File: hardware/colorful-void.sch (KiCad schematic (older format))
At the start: 4 parts, among them J1 Raspberry_Pi_Zero, J2 Barrel_Jack, J3 Conn_01x03, U1 74AHCT125

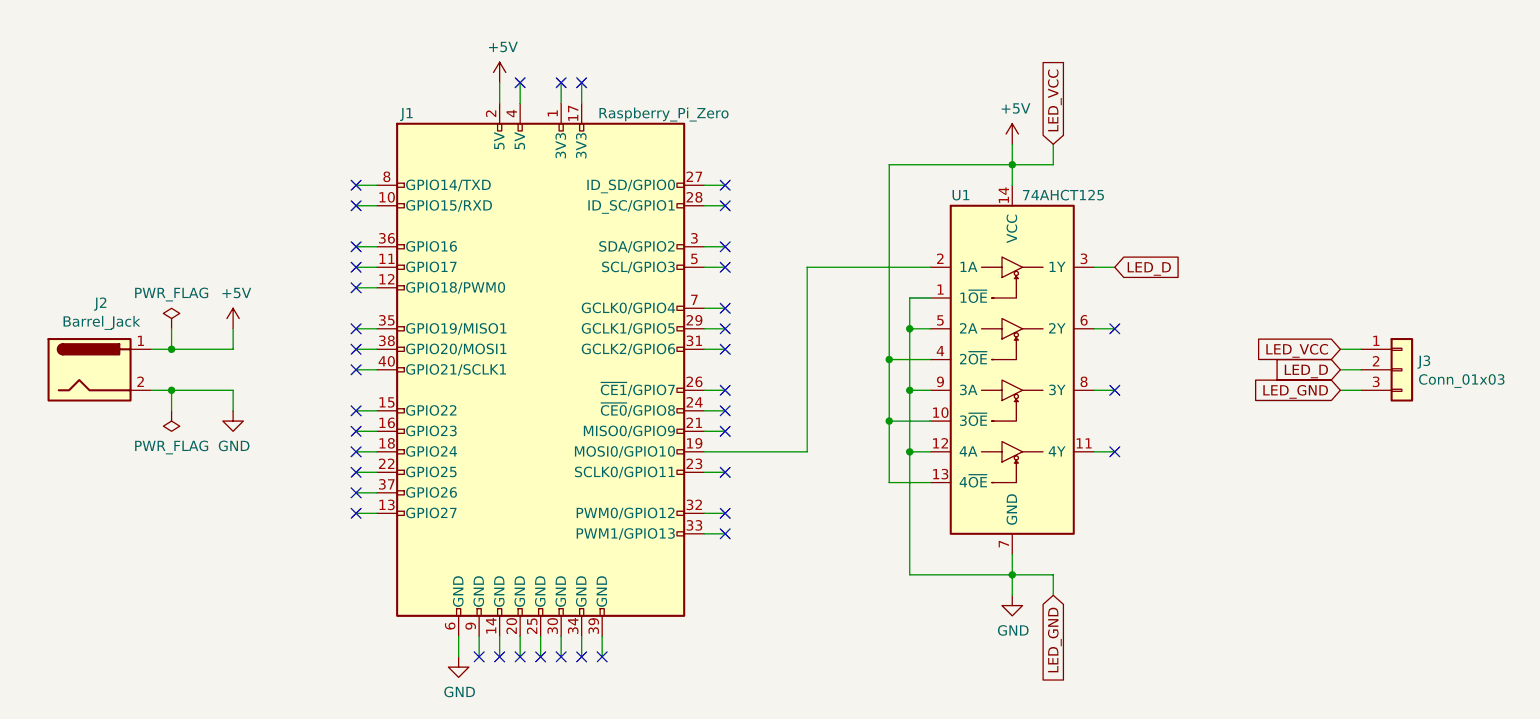
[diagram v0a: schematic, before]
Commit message: Connect client to RGB strip
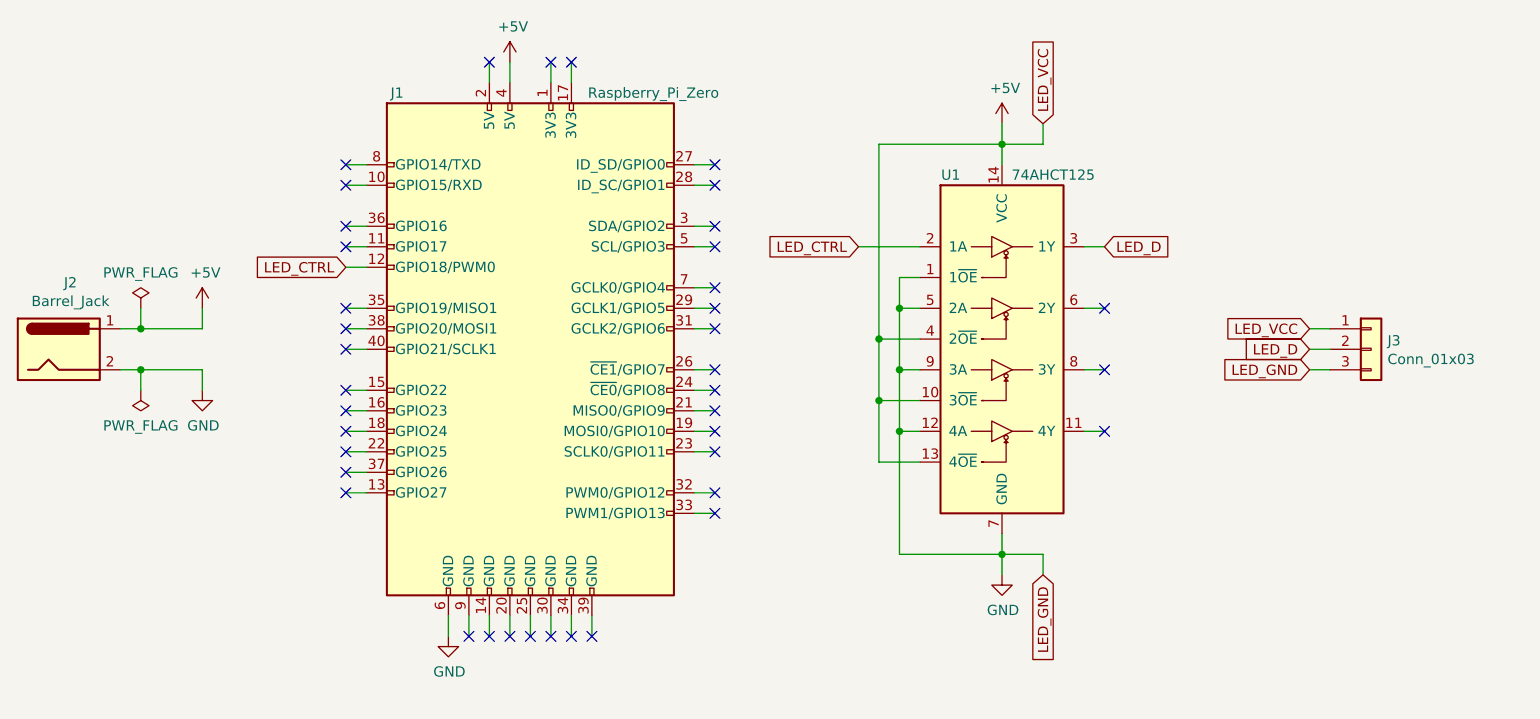
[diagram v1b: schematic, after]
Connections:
- net +5V: now also J1.4 (5V); no longer J1.2 (5V)
- net LED_CTRL: now reaches J1.12 (GPIO18/PWM0)
- net LED_CTRL: now also U1.2 (1A)
- net at J1.19 (MOSI0/GPIO10): no longer U1.2 (1A)
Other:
- moved on the sheet: J1, J2, J3, U1

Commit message: PCB rev. 1
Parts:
- removed J2: Barrel_Jack, symbol Connector:Barrel_Jack
- added H1, H2: MountingHole, misc_hardware:MountingHole_M2.5, symbol Mechanical:MountingHole
- added J2: Conn_01x02, misc_hardware:TerminalBlock_Kaweei_1x02_P2.54mm_Horizontal, symbol Connector_Generic:Conn_01x02
- added NT1: Net-Tie_2, NetTie:NetTie-2_SMD_Pad0.5mm, symbol Device:Net-Tie_2
- J1: footprint (none) -> Connector_PinHeader_2.54mm:PinHeader_2x06_P2.54mm_Vertical
- J3: footprint (none) -> misc_hardware:TerminalBlock_Kaweei_1x03_P2.54mm_Horizontal
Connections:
- net +5V: now also J2.2 (Pin_2), NT1.2; no longer U1.10 (3~OE), U1.13 (4~OE), U1.4 (2~OE)
- net GND: now also J3.2 (Pin_2), J2.1 (Pin_1); no longer J3.3 (Pin_3)
- net LED_D: now also J3.3 (Pin_3); no longer J3.2 (Pin_2)
- new net: NT1.1, U1.10 (3~OE), U1.13 (4~OE), U1.4 (2~OE)
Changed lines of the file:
@@
 F 0 "J1" H 4250 5050 50  0000 C CNN
 F 1 "Raspberry_Pi_Zero" H 5500 5050 50  0000 C CNN
-F 2 "" H 4900 3800 50  0001 C CNN
+F 2 "Connector_PinHeader_2.54mm:PinHeader_2x06_P2.54mm_Vertical" H 4900 3800 50  0001 C CNN
 F 3 "https://www.raspberrypi.org/documentation/hardware/raspberrypi/schematics/rpi_SCH_3bplus_1p0_reduced.pdf" H 4900 3800 50  0001 C CNN
 	1    4900 3800
@@
 	6700 3450 6700 3600
 Wire Wire Line
-	6700 4800 7200 4800
-Wire Wire Line
 	6700 3450 6800 3450
 Connection ~ 6700 3600
@@
 Connection ~ 6600 3750
 Wire Wire Line
-	6600 3750 6600 2800
+	6600 3750 6600 3100
 Connection ~ 6600 4050
 Wire Wire Line
@@
 NoConn ~ 5000 2400
 NoConn ~ 5100 2400
-$Comp
-L Connector:Barrel_Jack J2
-U 1 1 5FDE4F93
-P 2600 3800
-F 0 "J2" H 2657 4125 50  0000 C CNN
-F 1 "Barrel_Jack" H 2657 4034 50  0000 C CNN
-F 2 "" H 2650 3760 50  0001 C CNN
-F 3 "~" H 2650 3760 50  0001 C CNN
-	1    2600 3800
-	1    0    0    -1
-$EndComp
-Wire Wire Line
-	2900 3700 3000 3700
-Wire Wire Line
-	3000 3700 3000 3600
-Wire Wire Line
-	2900 3900 3000 3900
-Wire Wire Line
-	3000 3900 3000 4000
+Wire Wire Line
+	2900 3750 3000 3750
+Wire Wire Line
+	3000 3750 3000 3650
+Wire Wire Line
+	2900 3850 3000 3850
+Wire Wire Line
+	3000 3850 3000 3950
 $Comp
 L power:+5V #PWR03
 U 1 1 5FDEBA13
-P 3300 3600
-F 0 "#PWR03" H 3300 3450 50  0001 C CNN
-F 1 "+5V" H 3315 3773 50  0000 C CNN
-F 2 "" H 3300 3600 50  0001 C CNN
-F 3 "" H 3300 3600 50  0001 C CNN
-	1    3300 3600
+P 3300 3650
+F 0 "#PWR03" H 3300 3500 50  0001 C CNN
+F 1 "+5V" H 3315 3823 50  0000 C CNN
+F 2 "" H 3300 3650 50  0001 C CNN
+F 3 "" H 3300 3650 50  0001 C CNN
+	1    3300 3650
 	1    0    0    -1
 $EndComp
@@
 L power:GND #PWR04
 U 1 1 5FDEC1C7
-P 3300 4000
-F 0 "#PWR04" H 3300 3750 50  0001 C CNN
-F 1 "GND" H 3305 3827 50  0000 C CNN
-F 2 "" H 3300 4000 50  0001 C CNN
-F 3 "" H 3300 4000 50  0001 C CNN
-	1    3300 4000
+P 3300 3950
+F 0 "#PWR04" H 3300 3700 50  0001 C CNN
+F 1 "GND" H 3305 3777 50  0000 C CNN
+F 2 "" H 3300 3950 50  0001 C CNN
+F 3 "" H 3300 3950 50  0001 C CNN
+	1    3300 3950
 	1    0    0    -1
 $EndComp
@@
 L power:PWR_FLAG #FLG01
 U 1 1 5FDF5B6E
-P 3000 3600
-F 0 "#FLG01" H 3000 3675 50  0001 C CNN
-F 1 "PWR_FLAG" H 3000 3773 50  0000 C CNN
-F 2 "" H 3000 3600 50  0001 C CNN
-F 3 "~" H 3000 3600 50  0001 C CNN
-	1    3000 3600
-	1    0    0    -1
-$EndComp
-Wire Wire Line
-	3300 3600 3300 3700
-Wire Wire Line
-	3300 3700 3000 3700
-Connection ~ 3000 3700
-Wire Wire Line
-	3300 4000 3300 3900
-Wire Wire Line
-	3300 3900 3000 3900
-Connection ~ 3000 3900
+P 3000 3650
+F 0 "#FLG01" H 3000 3725 50  0001 C CNN
+F 1 "PWR_FLAG" H 3000 3823 50  0000 C CNN
+F 2 "" H 3000 3650 50  0001 C CNN
+F 3 "~" H 3000 3650 50  0001 C CNN
+	1    3000 3650
+	1    0    0    -1
+$EndComp
+Wire Wire Line
+	3300 3650 3300 3750
+Wire Wire Line
+	3300 3750 3000 3750
+Connection ~ 3000 3750
+Wire Wire Line
+	3300 3950 3300 3850
+Wire Wire Line
+	3300 3850 3000 3850
+Connection ~ 3000 3850
 $Comp
 L power:PWR_FLAG #FLG02
 U 1 1 5FDFB526
-P 3000 4000
-F 0 "#FLG02" H 3000 4075 50  0001 C CNN
-F 1 "PWR_FLAG" H 3000 4173 50  0000 C CNN
-F 2 "" H 3000 4000 50  0001 C CNN
-F 3 "~" H 3000 4000 50  0001 C CNN
-	1    3000 4000
+P 3000 3950
+F 0 "#FLG02" H 3000 4025 50  0001 C CNN
+F 1 "PWR_FLAG" H 3000 4123 50  0000 C CNN
+F 2 "" H 3000 3950 50  0001 C CNN
+F 3 "~" H 3000 3950 50  0001 C CNN
+	1    3000 3950
 	-1   0    0    1
 $EndComp
@@
 F 0 "J3" H 9080 3842 50  0000 L CNN
 F 1 "Conn_01x03" H 9080 3751 50  0000 L CNN
-F 2 "" H 9000 3800 50  0001 C CNN
+F 2 "misc_hardware:TerminalBlock_Kaweei_1x03_P2.54mm_Horizontal" H 9000 3800 50  0001 C CNN
 F 3 "~" H 9000 3800 50  0001 C CNN
 	1    9000 3800
@@
 Text GLabel 8700 3700 0    50   Input ~ 0
 LED_VCC
+Text GLabel 8700 3900 0    50   Input ~ 0
+LED_D
 Text GLabel 8700 3800 0    50   Input ~ 0
-LED_D
-Text GLabel 8700 3900 0    50   Input ~ 0
 LED_GND
 Wire Wire Line
@@
 	6500 3300 6800 3300
 NoConn ~ 4700 2400
+$Comp
+L Connector_Generic:Conn_01x02 J2
+U 1 1 5FEFCA38
+P 2700 3850
+F 0 "J2" H 2700 3650 50  0000 C CNN
+F 1 "Conn_01x02" H 2700 3950 50  0000 C CNN
+F 2 "misc_hardware:TerminalBlock_Kaweei_1x02_P2.54mm_Horizontal" H 2700 3850 50  0001 C CNN
+F 3 "~" H 2700 3850 50  0001 C CNN
+	1    2700 3850
+	-1   0    0    1
+$EndComp
+$Comp
+L Device:Net-Tie_2 NT1
+U 1 1 5FF0F2A7
+P 6600 3000
+F 0 "NT1" V 6650 3200 50  0000 R CNN
+F 1 "Net-Tie_2" V 6550 3450 50  0000 R CNN
+F 2 "NetTie:NetTie-2_SMD_Pad0.5mm" H 6600 3000 50  0001 C CNN
+F 3 "~" H 6600 3000 50  0001 C CNN
+	1    6600 3000
+	0    -1   -1   0
+$EndComp
+Wire Wire Line
+	6600 2900 6600 2800
+Wire Wire Line
+	6700 4800 7200 4800
+$Comp
+L Mechanical:MountingHole H1
+U 1 1 5FF4F0EB
+P 9000 4250
+F 0 "H1" H 9100 4296 50  0000 L CNN
+F 1 "MountingHole" H 9100 4205 50  0000 L CNN
+F 2 "misc_hardware:MountingHole_M2.5" H 9000 4250 50  0001 C CNN
+F 3 "~" H 9000 4250 50  0001 C CNN
+	1    9000 4250
+	1    0    0    -1
+$EndComp
+$Comp
+L Mechanical:MountingHole H2
+U 1 1 5FF5065F
+P 9000 4500
+F 0 "H2" H 9100 4546 50  0000 L CNN
+F 1 "MountingHole" H 9100 4455 50  0000 L CNN
+F 2 "misc_hardware:MountingHole_M2.5" H 9000 4500 50  0001 C CNN
+F 3 "~" H 9000 4500 50  0001 C CNN
+	1    9000 4500
+	1    0    0    -1
+$EndComp
 $EndSCHEMATC

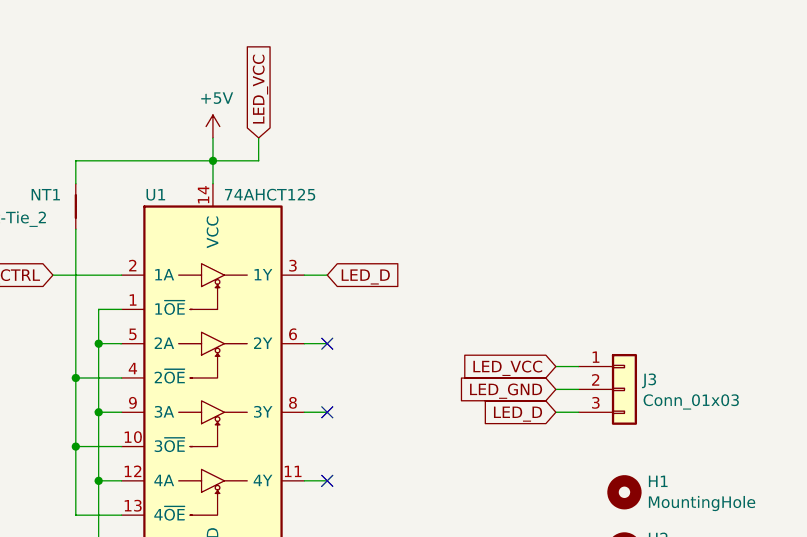
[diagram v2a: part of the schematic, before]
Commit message: Current limiting resistor on LED data line
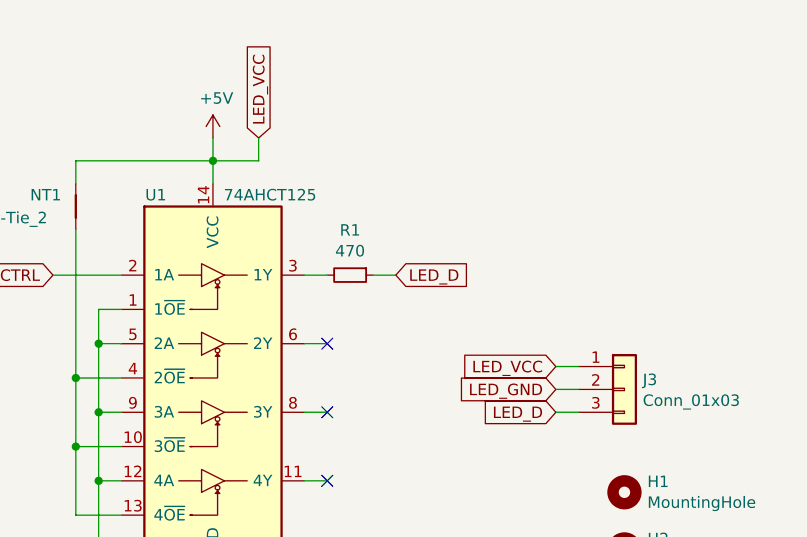
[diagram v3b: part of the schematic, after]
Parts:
- added R1: 470, Resistor_THT:R_Axial_DIN0309_L9.0mm_D3.2mm_P12.70mm_Horizontal, symbol Device:R_Small
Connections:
- net LED_D: now also R1.1; no longer U1.3 (1Y)
- new net: R1.2, U1.3 (1Y)
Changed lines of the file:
@@
 Wire Wire Line
 	7600 3300 7700 3300
-Text GLabel 7700 3300 2    50   Input ~ 0
-LED_D
 Wire Wire Line
 	7600 3600 7700 3600
@@
 NoConn ~ 5000 2400
 NoConn ~ 5100 2400
-Wire Wire Line
-	2900 3750 3000 3750
-Wire Wire Line
-	3000 3750 3000 3650
-Wire Wire Line
-	2900 3850 3000 3850
-Wire Wire Line
-	3000 3850 3000 3950
+$Comp
+L Connector_Generic:Conn_01x03 J3
+U 1 1 5FE0F243
+P 9000 3800
+F 0 "J3" H 9080 3842 50  0000 L CNN
+F 1 "Conn_01x03" H 9080 3751 50  0000 L CNN
+F 2 "misc_hardware:TerminalBlock_Kaweei_1x03_P2.54mm_Horizontal" H 9000 3800 50  0001 C CNN
+F 3 "~" H 9000 3800 50  0001 C CNN
+	1    9000 3800
+	1    0    0    -1
+$EndComp
+Wire Wire Line
+	8800 3700 8700 3700
+Wire Wire Line
+	8700 3800 8800 3800
+Wire Wire Line
+	8800 3900 8700 3900
+Text GLabel 8700 3700 0    50   Input ~ 0
+LED_VCC
+Text GLabel 8700 3900 0    50   Input ~ 0
+LED_D
+Text GLabel 8700 3800 0    50   Input ~ 0
+LED_GND
+Wire Wire Line
+	5800 4200 5700 4200
+NoConn ~ 5800 4200
+Text GLabel 6500 3300 0    50   Input ~ 0
+LED_CTRL
+Text GLabel 4000 3400 0    50   Input ~ 0
+LED_CTRL
+Wire Wire Line
+	4000 3400 4100 3400
+Wire Wire Line
+	6500 3300 6800 3300
+NoConn ~ 4700 2400
+$Comp
+L Device:Net-Tie_2 NT1
+U 1 1 5FF0F2A7
+P 6600 3000
+F 0 "NT1" V 6650 3200 50  0000 R CNN
+F 1 "Net-Tie_2" V 6550 3450 50  0000 R CNN
+F 2 "NetTie:NetTie-2_SMD_Pad0.5mm" H 6600 3000 50  0001 C CNN
+F 3 "~" H 6600 3000 50  0001 C CNN
+	1    6600 3000
+	0    -1   -1   0
+$EndComp
+Wire Wire Line
+	6600 2900 6600 2800
+Wire Wire Line
+	6700 4800 7200 4800
+$Comp
+L Mechanical:MountingHole H1
+U 1 1 5FF4F0EB
+P 9000 4250
+F 0 "H1" H 9100 4296 50  0000 L CNN
+F 1 "MountingHole" H 9100 4205 50  0000 L CNN
+F 2 "misc_hardware:MountingHole_M2.5" H 9000 4250 50  0001 C CNN
+F 3 "~" H 9000 4250 50  0001 C CNN
+	1    9000 4250
+	1    0    0    -1
+$EndComp
+$Comp
+L Mechanical:MountingHole H2
+U 1 1 5FF5065F
+P 9000 4500
+F 0 "H2" H 9100 4546 50  0000 L CNN
+F 1 "MountingHole" H 9100 4455 50  0000 L CNN
+F 2 "misc_hardware:MountingHole_M2.5" H 9000 4500 50  0001 C CNN
+F 3 "~" H 9000 4500 50  0001 C CNN
+	1    9000 4500
+	1    0    0    -1
+$EndComp
 $Comp
 L power:+5V #PWR03
@@
 	1    0    0    -1
 $EndComp
+Wire Wire Line
+	3300 3850 3000 3850
+Wire Wire Line
+	3300 3950 3300 3850
+Wire Wire Line
+	3300 3750 3000 3750
+Connection ~ 3000 3750
+Wire Wire Line
+	3300 3650 3300 3750
 $Comp
 L power:PWR_FLAG #FLG01
@@
 $EndComp
 Wire Wire Line
-	3300 3650 3300 3750
-Wire Wire Line
-	3300 3750 3000 3750
-Connection ~ 3000 3750
-Wire Wire Line
-	3300 3950 3300 3850
-Wire Wire Line
-	3300 3850 3000 3850
+	3000 3750 3000 3650
 Connection ~ 3000 3850
+Wire Wire Line
+	3000 3850 3000 3950
 $Comp
 L power:PWR_FLAG #FLG02
@@
 	-1   0    0    1
 $EndComp
-$Comp
-L Connector_Generic:Conn_01x03 J3
-U 1 1 5FE0F243
-P 9000 3800
-F 0 "J3" H 9080 3842 50  0000 L CNN
-F 1 "Conn_01x03" H 9080 3751 50  0000 L CNN
-F 2 "misc_hardware:TerminalBlock_Kaweei_1x03_P2.54mm_Horizontal" H 9000 3800 50  0001 C CNN
-F 3 "~" H 9000 3800 50  0001 C CNN
-	1    9000 3800
-	1    0    0    -1
-$EndComp
-Wire Wire Line
-	8800 3700 8700 3700
-Wire Wire Line
-	8700 3800 8800 3800
-Wire Wire Line
-	8800 3900 8700 3900
-Text GLabel 8700 3700 0    50   Input ~ 0
-LED_VCC
-Text GLabel 8700 3900 0    50   Input ~ 0
-LED_D
-Text GLabel 8700 3800 0    50   Input ~ 0
-LED_GND
-Wire Wire Line
-	5800 4200 5700 4200
-NoConn ~ 5800 4200
-Text GLabel 6500 3300 0    50   Input ~ 0
-LED_CTRL
-Text GLabel 4000 3400 0    50   Input ~ 0
-LED_CTRL
-Wire Wire Line
-	4000 3400 4100 3400
-Wire Wire Line
-	6500 3300 6800 3300
-NoConn ~ 4700 2400
+Wire Wire Line
+	2900 3750 3000 3750
+Wire Wire Line
+	2900 3850 3000 3850
 $Comp
 L Connector_Generic:Conn_01x02 J2
@@
 $EndComp
 $Comp
-L Device:Net-Tie_2 NT1
-U 1 1 5FF0F2A7
-P 6600 3000
-F 0 "NT1" V 6650 3200 50  0000 R CNN
-F 1 "Net-Tie_2" V 6550 3450 50  0000 R CNN
-F 2 "NetTie:NetTie-2_SMD_Pad0.5mm" H 6600 3000 50  0001 C CNN
-F 3 "~" H 6600 3000 50  0001 C CNN
-	1    6600 3000
-	0    -1   -1   0
-$EndComp
-Wire Wire Line
-	6600 2900 6600 2800
-Wire Wire Line
-	6700 4800 7200 4800
-$Comp
-L Mechanical:MountingHole H1
-U 1 1 5FF4F0EB
-P 9000 4250
-F 0 "H1" H 9100 4296 50  0000 L CNN
-F 1 "MountingHole" H 9100 4205 50  0000 L CNN
-F 2 "misc_hardware:MountingHole_M2.5" H 9000 4250 50  0001 C CNN
-F 3 "~" H 9000 4250 50  0001 C CNN
-	1    9000 4250
-	1    0    0    -1
-$EndComp
-$Comp
-L Mechanical:MountingHole H2
-U 1 1 5FF5065F
-P 9000 4500
-F 0 "H2" H 9100 4546 50  0000 L CNN
-F 1 "MountingHole" H 9100 4455 50  0000 L CNN
-F 2 "misc_hardware:MountingHole_M2.5" H 9000 4500 50  0001 C CNN
-F 3 "~" H 9000 4500 50  0001 C CNN
-	1    9000 4500
-	1    0    0    -1
-$EndComp
+L Device:R_Small R1
+U 1 1 5FFA7B48
+P 7800 3300
+F 0 "R1" V 7604 3300 50  0000 C CNN
+F 1 "470" V 7695 3300 50  0000 C CNN
+F 2 "Resistor_THT:R_Axial_DIN0309_L9.0mm_D3.2mm_P12.70mm_Horizontal" H 7800 3300 50  0001 C CNN
+F 3 "~" H 7800 3300 50  0001 C CNN
+	1    7800 3300
+	0    1    1    0
+$EndComp
+Wire Wire Line
+	7900 3300 8000 3300
+Text GLabel 8000 3300 2    50   Input ~ 0
+LED_D
 $EndSCHEMATC
